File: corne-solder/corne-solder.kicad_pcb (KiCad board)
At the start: 2 copper layers, 133.8 x 91.9 mm, 47 parts, among them J1 Battery Connector, J2 nice!view, SW1 SW_Push, SW10 SW_Push, SW11 SW_Push, SW12 SW_Push, SW13 SW_Push, SW14 SW_Push, SW15 SW_Push, SW16 SW_Push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

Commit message: update
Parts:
- D1, D10, D11, D12, D13, D14, D15, D16, D17, D18, D19, D2, D20, D21, D3, D4, D5, D6, D7, D8, D9: footprint Project:D_SOD-123F-Reversible-Solder -> Project:Diode-Reversible
- PSW1: moved to B.Cu
- moved D13 218.2 mm to (108.0, 98.2), turned to -90 degrees
- moved D19 209.5 mm to (153.5, 66.6), turned to 90 degrees
- moved D20 208.5 mm to (153.5, 85.6), turned to 90 degrees
- moved D21 190.9 mm to (129.0, 98.2), turned to -90 degrees
- moved D2 174.8 mm to (58.5, 69.0), turned to 90 degrees
- moved D3 173.8 mm to (58.5, 88.0), turned to 90 degrees
- moved D7 162.4 mm to (96.5, 45.2), turned to 90 degrees
- moved D8 161.3 mm to (96.5, 64.2), turned to 90 degrees
- moved D9 160.2 mm to (96.5, 83.2), turned to 90 degrees
- moved D14 155.0 mm to (134.5, 45.2), turned to 90 degrees
- moved D15 154.0 mm to (134.5, 64.2), turned to 90 degrees
- moved D16 153.0 mm to (134.5, 83.2), turned to 90 degrees
- moved D17 144.6 mm to (125.0, 98.2), turned to -90 degrees
- moved D4 112.7 mm to (77.5, 50.0), turned to 90 degrees
- moved D5 111.6 mm to (77.5, 69.0), turned to 90 degrees
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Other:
- outline, holes or cut-outs redrawn

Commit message: wiring
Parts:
- moved J1 155.7 mm to (169.0, 81.9), turned to -90 degrees
- moved RSW1 87.8 mm to (172.9, 86.2), turned to 90 degrees
- moved J2 2.54 mm to (164.6, 77.8)
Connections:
- J1 pad 1: Net-(J1-Pin_1) -> GND
- J1 pad 2: GND -> Net-(J1-Pin_2)
- PSW1 pad 2: Net-(J1-Pin_1) -> Net-(J1-Pin_2)
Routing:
- net row2: track 0.00 -> 138.7 mm
- net col0: track 0.00 -> 134.9 mm
- net row1: track 0.00 -> 122.3 mm
- net col1: track 0.00 -> 120.8 mm
- net row0: track 0.00 -> 110.2 mm
- net col2: track 0.00 -> 100.6 mm
- net col3: track 0.00 -> 96.4 mm
- net row3: track 0.00 -> 76.8 mm, vias 0 -> 1
- net col4: track 0.00 -> 76.5 mm
- net col5: track 0.00 -> 62.4 mm
- net Net-(J1-Pin_2): track 0.00 -> 45.0 mm, vias 0 -> 1
- net VCC: track 0.00 -> 38.5 mm
- net RST: track 0.00 -> 34.2 mm
- net Net-(D21-A): track 0.00 -> 32.0 mm
- net SDA: track 0.00 -> 30.2 mm, vias 0 -> 1
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- added copper zone on B.Cu, net GND
- added copper zone on F.Cu, net GND
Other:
- outline, holes or cut-outs redrawn

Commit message: more wiring and DRC
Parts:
- moved RSW1 1.91 mm to (172.9, 88.1)
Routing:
- net GND: track 15.0 -> 54.9 mm
- net col5: track 62.4 -> 74.0 mm
- net col3: track 96.4 -> 108.0 mm
- net col4: track 76.5 -> 88.1 mm
- net col2: track 100.6 -> 112.2 mm
- net row0: track 110.2 -> 121.5 mm
- net CS: track 16.5 -> 27.5 mm
- net RST: track 34.2 -> 43.8 mm, vias 0 -> 1
- net col0: track 134.9 -> 144.3 mm, vias 0 -> 1
- net col1: track 120.8 -> 130.2 mm, vias 0 -> 1
- net SDA: track 30.2 -> 38.2 mm, vias 1 -> 2
- net SCL: track 20.6 -> 28.3 mm, vias 1 -> 2
- net Net-(J1-Pin_2): track 45.0 -> 51.7 mm
- net RAW: track 7.79 -> 14.4 mm, vias 0 -> 1
- net VCC: track 38.5 -> 44.8 mm, vias 0 -> 1
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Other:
- outline, holes or cut-outs redrawn

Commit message: Update corne-solder.kicad_pcb
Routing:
- net GND: track 54.9 -> 56.7 mm, vias 2 -> 4
- net col3: track 108.0 -> 107.0 mm
- net VCC: track 44.8 -> 44.1 mm
- net SCL: track 28.3 -> 28.9 mm

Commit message: Update corne-solder.kicad_pcb
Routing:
- net SDA: track 37.8 -> 36.5 mm
- net GND: vias 4 -> 3
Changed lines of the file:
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@@
 		(pad_to_mask_clearance 0)
 		(allow_soldermask_bridges_in_footprints no)
-		(grid_origin 135.5 55.9375)
+		(grid_origin 164.625 60.05)
 		(pcbplotparams
 			(layerselection 0x00010fc_ffffffff)
@@
 	)
 	(segment
-		(start 163.355 71.48)
-		(end 163.355 74.625)
+		(start 162.72 48.62)
+		(end 160.18 51.16)
 		(width 0.3)
 		(layer "F.Cu")
@@
 	)
 	(segment
-		(start 162.72 48.62)
-		(end 160.18 51.16)
+		(start 163.355 72.115)
+		(end 163.355 74.625)
 		(width 0.3)
 		(layer "F.Cu")
@@
 	)
 	(via
-		(at 160.18 72.75)
-		(size 0.6)
-		(drill 0.3)
-		(layers "F.Cu" "B.Cu")
-		(net 27)
-	)
-	(via
-		(at 163.355 71.48)
+		(at 163.355 72.115)
 		(size 0.6)
 		(drill 0.3)
@@
 	)
 	(segment
-		(start 163.355 71.48)
-		(end 164.625 71.48)
+		(start 164.625 48.62)
+		(end 166.53 48.62)
 		(width 0.3)
 		(layer "B.Cu")
@@
 	)
 	(segment
-		(start 164.625 48.62)
-		(end 166.53 48.62)
+		(start 163.99 71.48)
+		(end 165.26 71.48)
 		(width 0.3)
 		(layer "B.Cu")
@@
 	)
 	(segment
+		(start 165.895 72.115)
+		(end 165.895 74.625)
+		(width 0.3)
+		(layer "B.Cu")
+		(net 27)
+	)
+	(segment
+		(start 163.355 72.115)
+		(end 163.99 71.48)
+		(width 0.3)
+		(layer "B.Cu")
+		(net 27)
+	)
+	(segment
 		(start 169.07 51.16)
 		(end 169.07 53.7)
@@
 	)
 	(segment
-		(start 166.53 48.62)
-		(end 169.07 51.16)
+		(start 165.26 71.48)
+		(end 165.895 72.115)
 		(width 0.3)
 		(layer "B.Cu")
@@
 	)
 	(segment
-		(start 165.895 72.75)
-		(end 165.895 74.625)
-		(width 0.3)
-		(layer "B.Cu")
-		(net 27)
-	)
-	(segment
-		(start 164.625 71.48)
-		(end 165.895 72.75)
+		(start 166.53 48.62)
+		(end 169.07 51.16)
 		(width 0.3)
 		(layer "B.Cu")
@@
 	)
 	(segment
-		(start 166.53 61.955)
-		(end 170.34 65.765)
+		(start 170.34 75.29)
+		(end 171.61 76.56)
 		(width 0.3)
 		(layer "F.Cu")
@@
 	)
 	(segment
-		(start 171.61 76.56)
-		(end 171.61 78.465)
+		(start 166.53 58.78)
+		(end 170.34 62.59)
 		(width 0.3)
 		(layer "F.Cu")
@@
 	)
 	(segment
-		(start 169.07 53.7)
-		(end 166.53 53.7)
+		(start 171.61 76.56)
+		(end 171.61 78.465)
 		(width 0.3)
 		(layer "F.Cu")
@@
 	)
 	(segment
-		(start 170.34 65.765)
-		(end 170.34 75.29)
+		(start 169.07 53.7)
+		(end 166.53 53.7)
 		(width 0.3)
 		(layer "F.Cu")
@@
 	)
 	(segment
-		(start 170.34 75.29)
-		(end 171.61 76.56)
+		(start 170.34 62.59)
+		(end 170.34 75.29)
 		(width 0.3)
 		(layer "F.Cu")
@@
 	)
 	(segment
-		(start 166.53 53.7)
-		(end 166.53 61.955)
+		(start 170.34 79.735)
+		(end 166.53 79.735)
 		(width 0.3)
 		(layer "F.Cu")
@@
 	)
 	(segment
-		(start 170.34 79.735)
-		(end 166.53 79.735)
+		(start 166.53 53.7)
+		(end 166.53 58.78)
 		(width 0.3)
 		(layer "F.Cu")
@@
 	)
 	(segment
-		(start 162.085 65.13)
-		(end 162.085 56.875)
+		(start 164.625 70.21)
+		(end 168.435 74.02)
 		(width 0.2)
 		(layer "F.Cu")
@@
 	)
 	(segment
-		(start 165.895 70.21)
-		(end 165.895 68.94)
-		(width 0.2)
-		(layer "F.Cu")
-		(net 31)
-	)
-	(segment
-		(start 165.895 68.94)
-		(end 162.085 65.13)
+		(start 162.085 67.67)
+		(end 162.085 56.875)
 		(width 0.2)
 		(layer "F.Cu")
@@
 	)
 	(segment
-		(start 165.895 71.48)
-		(end 168.435 74.02)
-		(width 0.2)
-		(layer "F.Cu")
-		(net 31)
-	)
-	(segment
-		(start 165.895 70.21)
-		(end 165.895 71.48)
+		(start 164.625 70.21)
+		(end 162.085 67.67)
 		(width 0.2)
 		(layer "F.Cu")
@@
 	)
 	(via
-		(at 165.895 70.21)
+		(at 164.625 70.21)
 		(size 0.6)
 		(drill 0.3)
@@
 	)
 	(segment
-		(start 160.815 72.75)
-		(end 160.815 74.625)
+		(start 168.435 56.875)
+		(end 169.07 56.24)
 		(width 0.2)
 		(layer "B.Cu")
@@
 	)
 	(segment
-		(start 163.355 70.21)
-		(end 160.815 72.75)
+		(start 164.625 70.21)
+		(end 163.355 70.21)
 		(width 0.2)
 		(layer "B.Cu")
@@
 	)
 	(segment
-		(start 168.435 56.875)
-		(end 169.07 56.24)
+		(start 160.815 72.75)
+		(end 160.815 74.625)
 		(width 0.2)
 		(layer "B.Cu")
@@
 	)
 	(segment
-		(start 165.895 70.21)
-		(end 163.355 70.21)
+		(start 163.355 70.21)
+		(end 160.815 72.75)
 		(width 0.2)
 		(layer "B.Cu")
@@
 	)
 	(segment
+		(start 161.45 68.305)
+		(end 161.45 59.415)
+		(width 0.2)
+		(layer "F.Cu")
+		(net 32)
+	)
+	(segment
 		(start 161.45 59.415)
 		(end 160.815 59.415)
@@
 	)
 	(segment
-		(start 164.625 72.75)
-		(end 164.625 68.305)
+		(start 164.625 71.48)
+		(end 161.45 68.305)
 		(width 0.2)
 		(layer "F.Cu")
@@
 	)
 	(segment
-		(start 161.45 65.13)
-		(end 161.45 59.415)
+		(start 164.625 72.75)
+		(end 164.625 71.48)
 		(width 0.2)
 		(layer "F.Cu")
@@
 		(net 32)
 	)
-	(segment
-		(start 164.625 68.305)
-		(end 161.45 65.13)
-		(width 0.2)
-		(layer "F.Cu")
-		(net 32)
-	)
 	(via
 		(at 164.625 72.75)
@@
 	)
 	(segment
-		(start 50 80.38)
-		(end 47.46 82.92)
+		(start 168.435 55.605)
+		(end 169.07 56.24)
 		(width 0.2)
 		(layer "F.Cu")
@@
 	)
 	(segment
-		(start 167.8 55.605)
-		(end 168.435 55.605)
+		(start 50 80.38)
+		(end 47.46 82.92)
 		(width 0.2)
 		(layer "F.Cu")
@@
 	)
 	(segment
-		(start 168.435 55.605)
-		(end 169.07 56.24)
+		(start 167.8 55.605)
+		(end 168.435 55.605)
 		(width 0.2)
 		(layer "F.Cu")
@@
 	)
 	(segment
+		(start 167.8 55.605)
+		(end 160.815 55.605)
+		(width 0.2)
+		(layer "B.Cu")
+		(net 36)
+	)
+	(segment
 		(start 60.024314 55.9)
 		(end 62.024314 57.9)
@@
 	)
 	(segment
-		(start 167.8 55.605)
-		(end 160.815 55.605)
+		(start 160.815 55.605)
+		(end 160.18 56.24)
 		(width 0.2)
 		(layer "B.Cu")
@@
 		(width 0.2)
 		(layer "B.Cu")
-		(net 36)
-	)
-	(segment
-		(start 160.815 55.605)
-		(end 160.18 56.24)
-		(width 0.2)
-		(layer "B.Cu")

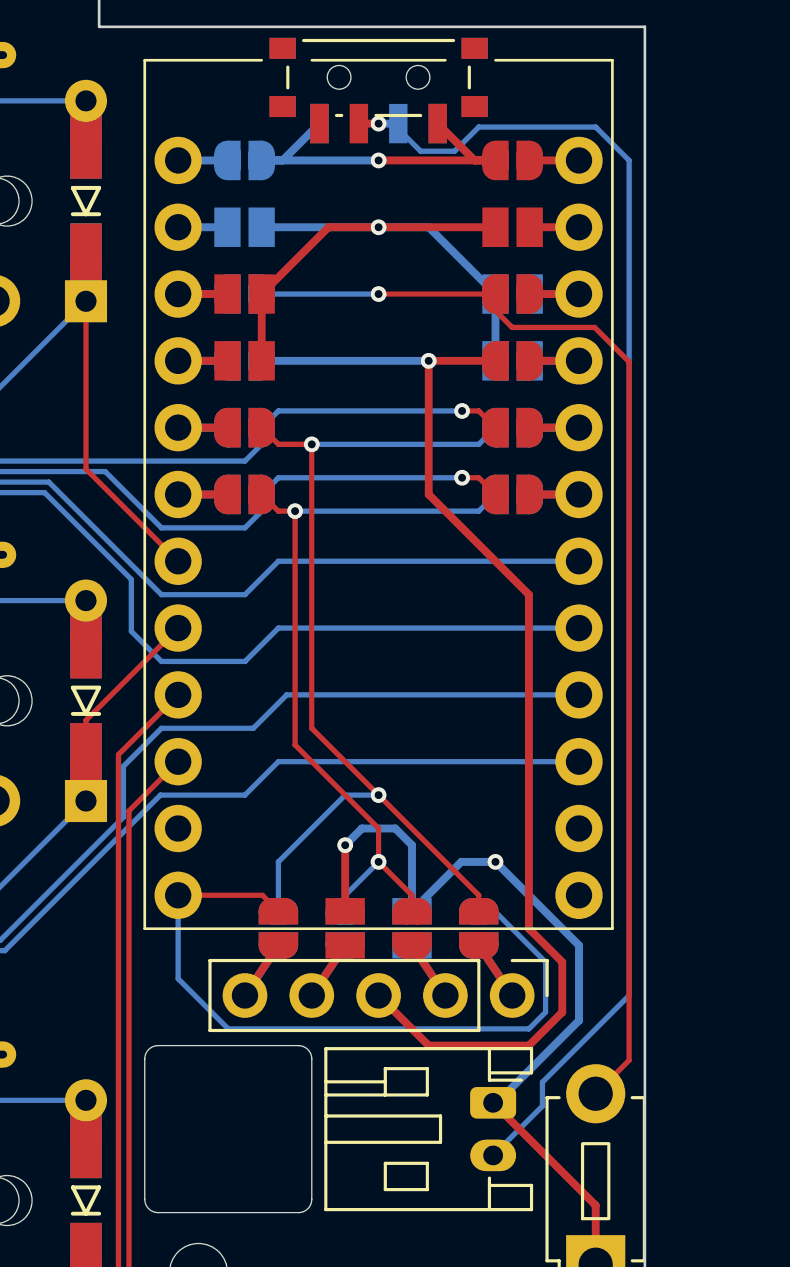
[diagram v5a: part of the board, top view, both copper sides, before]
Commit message: move niceview jump pads
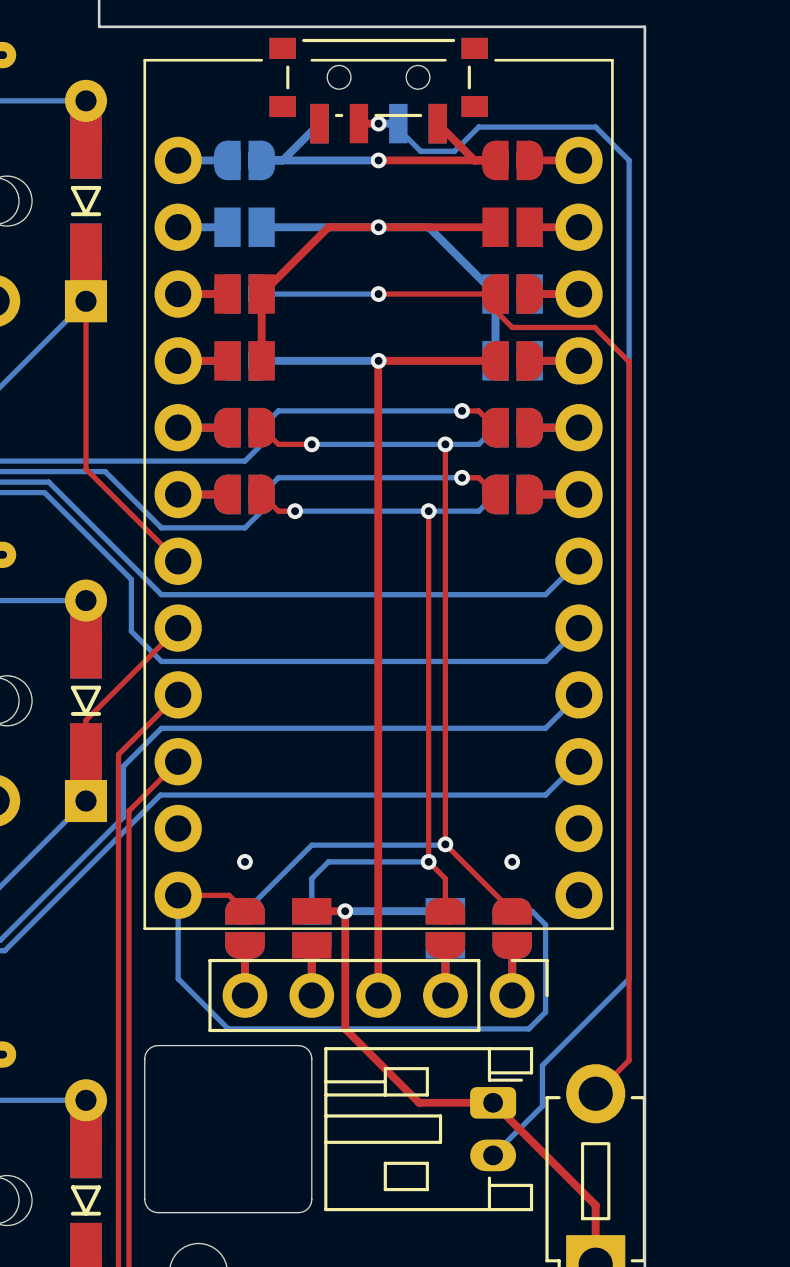
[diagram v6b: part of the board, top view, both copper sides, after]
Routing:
- net VCC: track 44.1 -> 33.0 mm
- net GND: track 56.7 -> 49.1 mm, vias 3 -> 4
- net SCL: track 28.9 -> 30.8 mm, vias 2 -> 3
- net CS: track 27.5 -> 25.8 mm
- net SDA: track 36.5 -> 36.9 mm, vias 2 -> 3

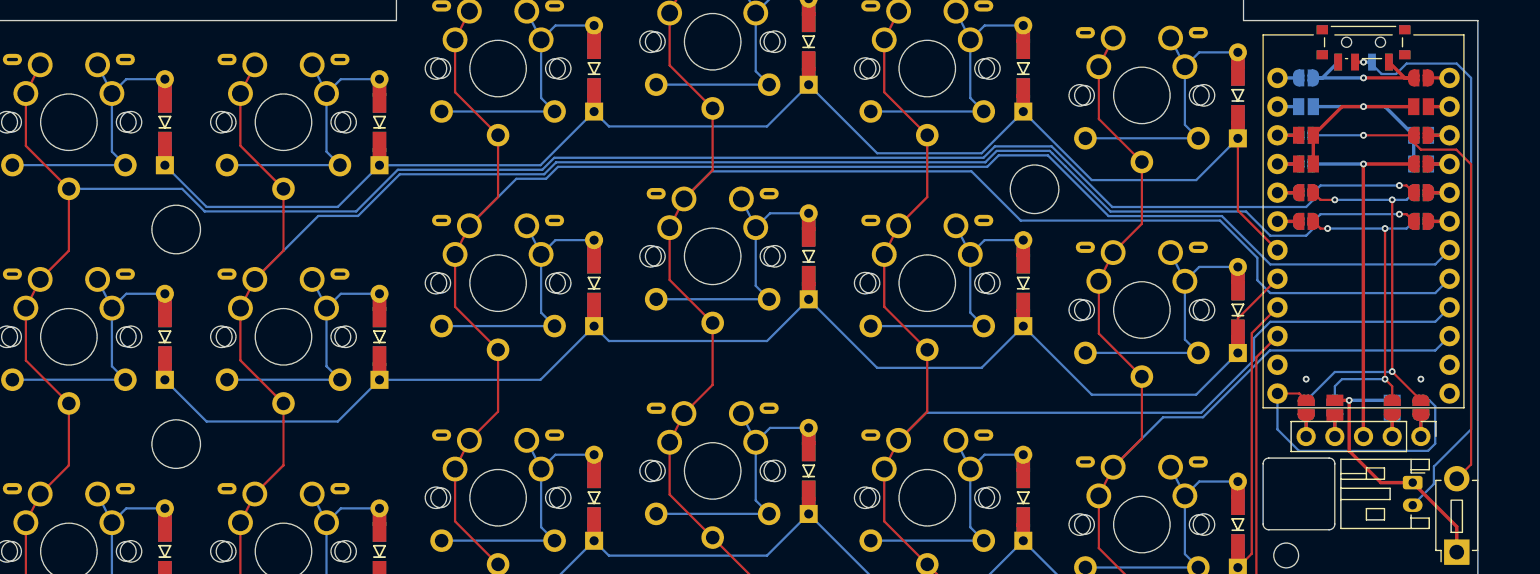
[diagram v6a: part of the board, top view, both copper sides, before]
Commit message: jump pads edit
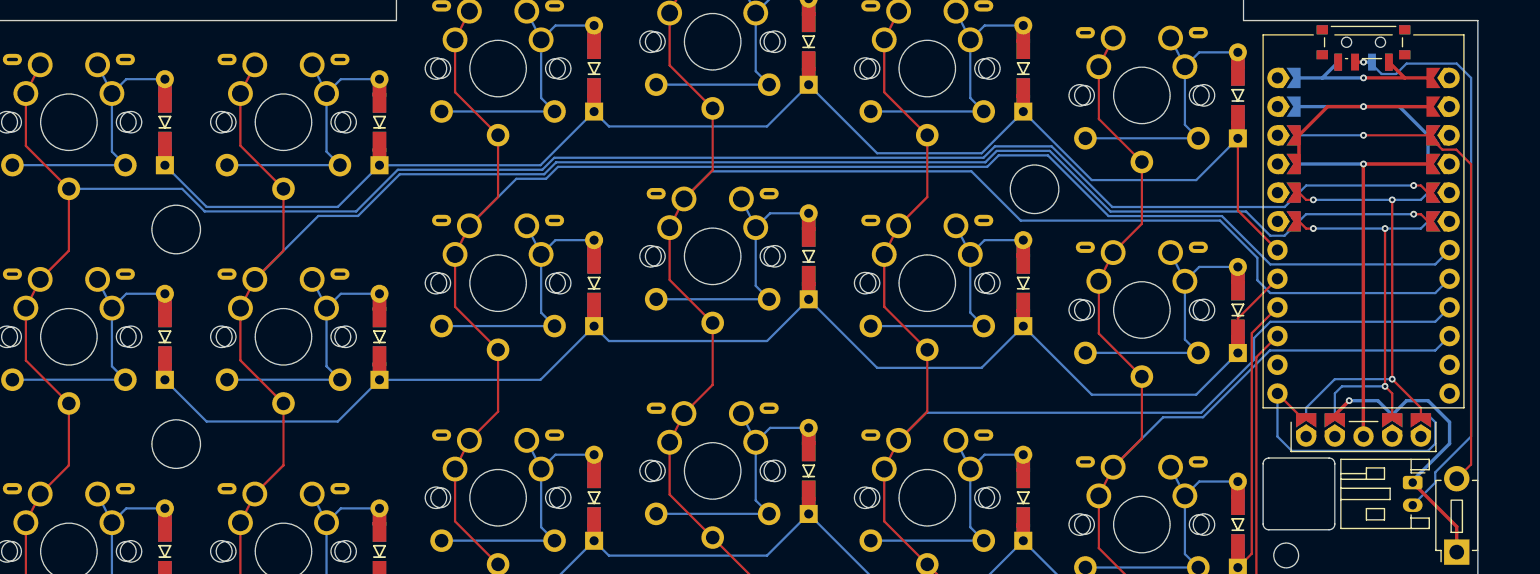
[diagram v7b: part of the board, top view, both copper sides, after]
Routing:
- net GND: track 49.1 -> 57.0 mm, vias 4 -> 2
- net SCL: track 30.8 -> 35.3 mm
- net SDA: track 36.9 -> 41.4 mm
- net VCC: track 33.0 -> 35.6 mm
- net RAW: track 14.4 -> 15.4 mm
- net col0: track 144.1 -> 145.0 mm
- net RST: track 43.8 -> 44.7 mm
- net col1: track 130.0 -> 130.9 mm

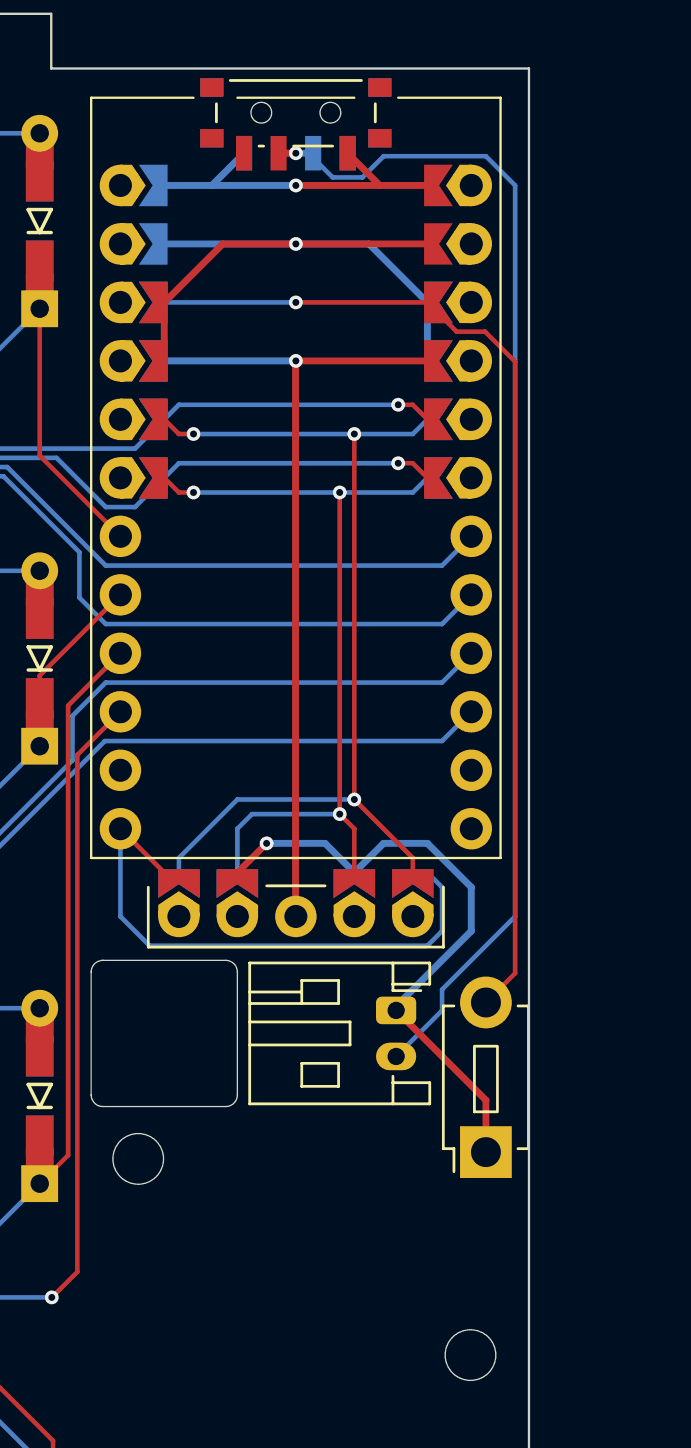
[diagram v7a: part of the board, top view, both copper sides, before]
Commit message: More jump pads
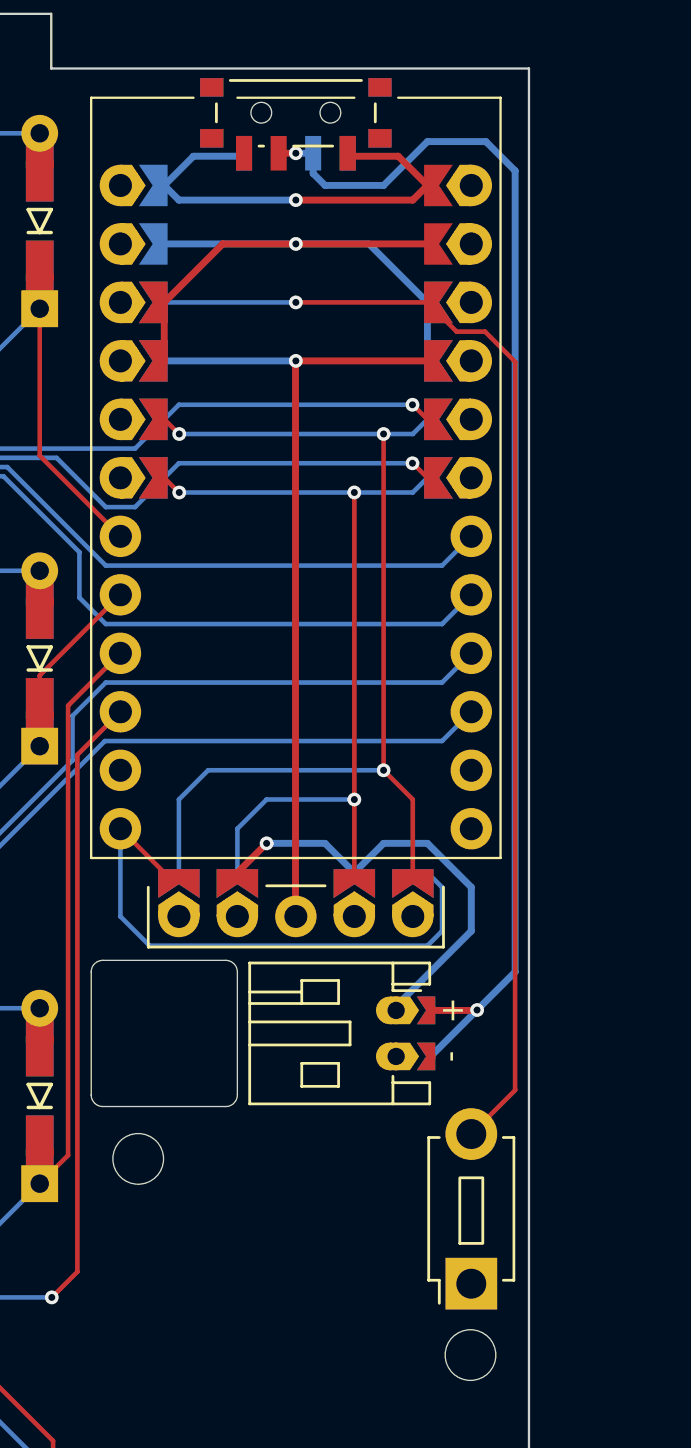
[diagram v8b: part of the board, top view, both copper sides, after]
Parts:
- J1: footprint Connector_JST:JST_PH_S2B-PH-K_1x02_P2.00mm_Horizontal -> Project:JST_PH_S2B-PH-K_1x02_P2.00mm_Horizontal
- moved RSW1 5.75 mm to (172.2, 93.8)
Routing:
- net GND: track 57.0 -> 49.3 mm
- net RST: track 44.7 -> 50.6 mm
- net RAW: track 15.4 -> 20.0 mm
- net Net-(J1-Pin_2): track 51.7 -> 54.7 mm, vias 1 -> 2
- net SDA: track 41.4 -> 44.1 mm
- net SCL: track 35.3 -> 36.0 mm
